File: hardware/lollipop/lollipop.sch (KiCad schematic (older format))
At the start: 24 parts

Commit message: filter/balun bom info
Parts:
- removed T? (x3): BALUN, symbol BALUN
- removed U?: FIL-DEA, symbol FIL-DEA
- removed U?: FIL-LP0603, symbol FIL-LP0603
- added T? (x3): BALUN, symbol BALUN
- added U?: FIL-DEA, symbol FIL-DEA
- added U?: FIL-LP0603, symbol FIL-LP0603
- T?: Description (none) -> BALUN CERAMIC CHIP WIMAX 2.5GHZ; Manufacturer (none) -> Johanson Technology; Part Number (none) -> 2500BL14M100T
- T?: Description (none) -> TRANSFORMR BALUN 2.3-2700MHZ SMD; Manufacturer (none) -> Pulse Electronics; Part Number (none) -> CX2156NL
- T?: Description (none) -> XFMR BALUN RF 3.0-8.0GHZ UWB SMD; Manufacturer (none) -> TDK; Part Number (none) -> HHM1595A1
- U?: Description (none) -> FILTER HIGHPASS WLAN&BLUETOOTH; Manufacturer (none) -> TDK; Part Number (none) -> DEA162400HT-8004B1
- U?: Description (none) -> FILTER LOW PASS 1880MHZ 0603 SMD; Manufacturer (none) -> AVX; Part Number (none) -> LP0603A1880ANTR
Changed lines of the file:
@@
-EESchema Schematic File Version 2  date Sun Apr 22 21:56:01 2012
+EESchema Schematic File Version 2  date Sun Apr 22 22:13:19 2012
 LIBS:power
 LIBS:device
@@
 Comment4 ""
 $EndDescr
+$Comp
+L BALUN T?
+U 1 1 4F94D6C4
+P 7600 6300
+F 0 "T?" H 7600 6550 70  0000 C CNN
+F 1 "BALUN" H 7600 6000 70  0000 C CNN
+F 4 "Pulse Electronics" H 7600 6300 60  0001 C CNN "Manufacturer"
+F 5 "CX2156NL" H 7600 6300 60  0001 C CNN "Part Number"
+F 6 "TRANSFORMR BALUN 2.3-2700MHZ SMD" H 7600 6300 60  0001 C CNN "Description"
+	1    7600 6300
+	-1   0    0    1
+$EndComp
+$Comp
+L BALUN T?
+U 1 1 4F94D601
+P 7600 5500
+F 0 "T?" H 7600 5750 70  0000 C CNN
+F 1 "BALUN" H 7600 5200 70  0000 C CNN
+F 4 "TDK" H 7600 5500 60  0001 C CNN "Manufacturer"
+F 5 "HHM1595A1" H 7600 5500 60  0001 C CNN "Part Number"
+F 6 "XFMR BALUN RF 3.0-8.0GHZ UWB SMD" H 7600 5500 60  0001 C CNN "Description"
+	1    7600 5500
+	-1   0    0    1
+$EndComp
+$Comp
+L BALUN T?
+U 1 1 4F94D59C
+P 7600 7100
+F 0 "T?" H 7600 7350 70  0000 C CNN
+F 1 "BALUN" H 7600 6800 70  0000 C CNN
+F 4 "Johanson Technology" H 7600 7100 60  0001 C CNN "Manufacturer"
+F 5 "2500BL14M100T" H 7600 7100 60  0001 C CNN "Part Number"
+F 6 "BALUN CERAMIC CHIP WIMAX 2.5GHZ" H 7600 7100 60  0001 C CNN "Description"
+	1    7600 7100
+	-1   0    0    1
+$EndComp
+$Comp
+L FIL-LP0603 U?
+U 1 1 4F94D561
+P 6300 6250
+F 0 "U?" H 6300 6300 60  0000 C CNN
+F 1 "FIL-LP0603" H 6300 6200 60  0000 C CNN
+F 4 "AVX" H 6300 6250 60  0001 C CNN "Manufacturer"
+F 5 "LP0603A1880ANTR" H 6300 6250 60  0001 C CNN "Part Number"
+F 6 "FILTER LOW PASS 1880MHZ 0603 SMD" H 6300 6250 60  0001 C CNN "Description"
+	1    6300 6250
+	1    0    0    -1
+$EndComp
+$Comp
+L FIL-DEA U?
+U 1 1 4F94D4F4
+P 6300 5450
+F 0 "U?" H 6300 5500 60  0000 C CNN
+F 1 "FIL-DEA" H 6300 5400 60  0000 C CNN
+F 4 "TDK" H 6300 5450 60  0001 C CNN "Manufacturer"
+F 5 "DEA162400HT-8004B1" H 6300 5450 60  0001 C CNN "Part Number"
+F 6 "FILTER HIGHPASS WLAN&BLUETOOTH" H 6300 5450 60  0001 C CNN "Description"
+	1    6300 5450
+	1    0    0    -1
+$EndComp
 Text Notes 10200 5950 1    400  ~ 0
 mixer
@@
 $Comp
 L FIL-LP0603 U?
-U 1 1 4F94CF87
-P 6300 6250
-F 0 "U?" H 6300 6300 60  0000 C CNN
-F 1 "FIL-LP0603" H 6300 6200 60  0000 C CNN
-	1    6300 6250
-	1    0    0    -1
-$EndComp
-$Comp
-L FIL-DEA U?
-U 1 1 4F94CF80
-P 6300 5450
-F 0 "U?" H 6300 5500 60  0000 C CNN
-F 1 "FIL-DEA" H 6300 5400 60  0000 C CNN
-	1    6300 5450
-	1    0    0    -1
-$EndComp
-$Comp
-L FIL-LP0603 U?
 U 1 1 4F94CF46
 P 6300 3850
 F 0 "U?" H 6300 3900 60  0000 C CNN
 F 1 "FIL-LP0603" H 6300 3800 60  0000 C CNN
+F 4 "AVX" H 6300 3850 60  0001 C CNN "Manufacturer"
+F 5 "LP0603A1880ANTR" H 6300 3850 60  0001 C CNN "Part Number"
+F 6 "FILTER LOW PASS 1880MHZ 0603 SMD" H 6300 3850 60  0001 C CNN "Description"
 	1    6300 3850
 	1    0    0    -1
@@
 F 0 "U?" H 6300 4700 60  0000 C CNN
 F 1 "FIL-DEA" H 6300 4600 60  0000 C CNN
+F 4 "TDK" H 6300 4650 60  0001 C CNN "Manufacturer"
+F 5 "DEA162400HT-8004B1" H 6300 4650 60  0001 C CNN "Part Number"
+F 6 "FILTER HIGHPASS WLAN&BLUETOOTH" H 6300 4650 60  0001 C CNN "Description"
 	1    6300 4650
 	1    0    0    -1
@@
 $Comp
 L BALUN T?
-U 1 1 4F94CC80
-P 7600 7100
-F 0 "T?" H 7600 7350 70  0000 C CNN
-F 1 "BALUN" H 7600 6800 70  0000 C CNN
-	1    7600 7100
-	-1   0    0    1
-$EndComp
-$Comp
-L BALUN T?
-U 1 1 4F94CC7C
-P 7600 6300
-F 0 "T?" H 7600 6550 70  0000 C CNN
-F 1 "BALUN" H 7600 6000 70  0000 C CNN
-	1    7600 6300
-	-1   0    0    1
-$EndComp
-$Comp
-L BALUN T?
-U 1 1 4F94CC75
-P 7600 5500
-F 0 "T?" H 7600 5750 70  0000 C CNN
-F 1 "BALUN" H 7600 5200 70  0000 C CNN
-	1    7600 5500
-	-1   0    0    1
-$EndComp
-$Comp
-L BALUN T?
 U 1 1 4F94CC6F
 P 7600 4700
 F 0 "T?" H 7600 4950 70  0000 C CNN
 F 1 "BALUN" H 7600 4400 70  0000 C CNN
+F 4 "TDK" H 7600 4700 60  0001 C CNN "Manufacturer"
+F 5 "HHM1595A1" H 7600 4700 60  0001 C CNN "Part Number"
+F 6 "XFMR BALUN RF 3.0-8.0GHZ UWB SMD" H 7600 4700 60  0001 C CNN "Description"
 	1    7600 4700
 	-1   0    0    1
@@
 F 0 "T?" H 7600 4150 70  0000 C CNN
 F 1 "BALUN" H 7600 3600 70  0000 C CNN
+F 4 "Pulse Electronics" H 7600 3900 60  0001 C CNN "Manufacturer"
+F 5 "CX2156NL" H 7600 3900 60  0001 C CNN "Part Number"
+F 6 "TRANSFORMR BALUN 2.3-2700MHZ SMD" H 7600 3900 60  0001 C CNN "Description"
 	1    7600 3900
 	-1   0    0    1
@@
 F 0 "T?" H 7600 3350 70  0000 C CNN
 F 1 "BALUN" H 7600 2800 70  0000 C CNN
+F 4 "Johanson Technology" H 7600 3100 60  0001 C CNN "Manufacturer"
+F 5 "2500BL14M100T" H 7600 3100 60  0001 C CNN "Part Number"
+F 6 "BALUN CERAMIC CHIP WIMAX 2.5GHZ" H 7600 3100 60  0001 C CNN "Description"
 	1    7600 3100
 	-1   0    0    1

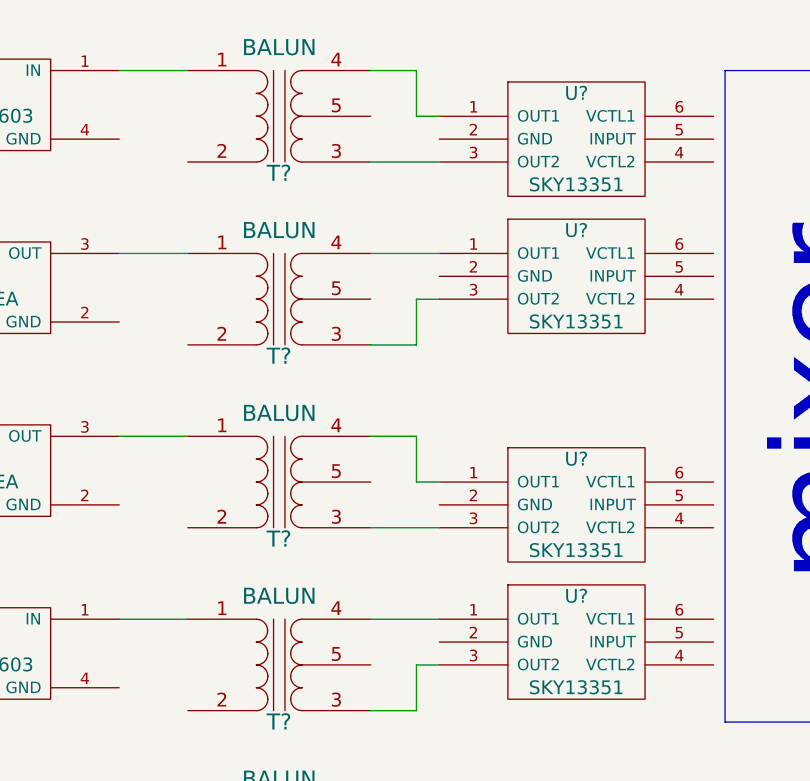
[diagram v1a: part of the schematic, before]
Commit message: fixed balun wiring
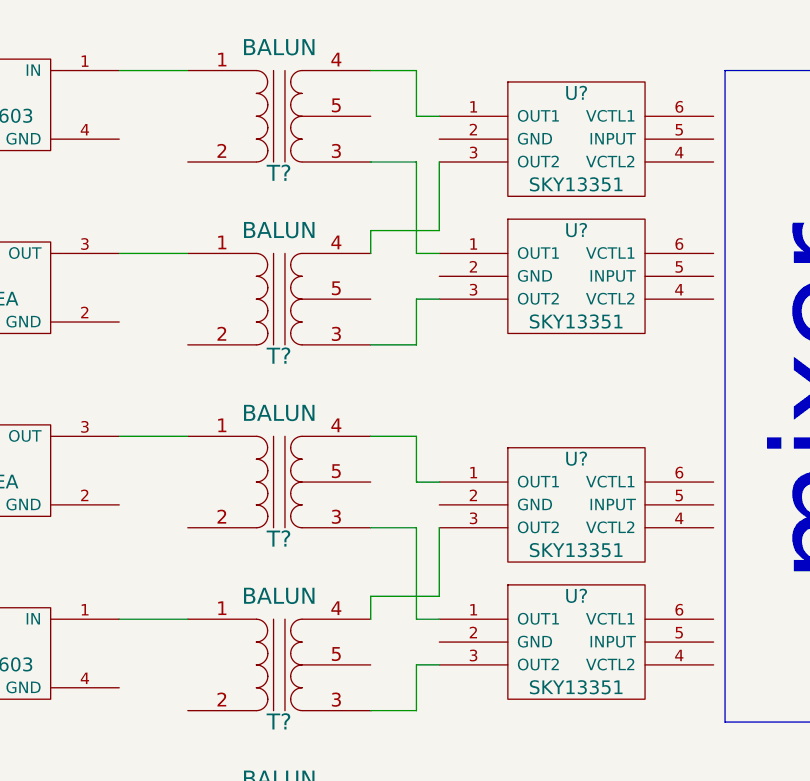
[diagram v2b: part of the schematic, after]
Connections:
- wire segments 69 -> 77
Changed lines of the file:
@@
-EESchema Schematic File Version 2  date Sun Apr 22 22:13:19 2012
+EESchema Schematic File Version 2  date Sun Apr 22 22:20:53 2012
 LIBS:power
 LIBS:device
@@
 Comment4 ""
 $EndDescr
+Wire Wire Line
+	8000 6100 8000 6000
+Wire Wire Line
+	8000 6000 8300 6000
+Wire Wire Line
+	8300 6000 8300 5700
+Wire Wire Line
+	8000 4500 8000 4400
+Wire Wire Line
+	8000 4400 8300 4400
+Wire Wire Line
+	8300 4400 8300 4100
+Wire Bus Line
+	10500 3700 9550 3700
+Wire Bus Line
+	10500 3700 10500 6550
+Wire Bus Line
+	10500 6550 9550 6550
+Wire Bus Line
+	9550 6550 9550 3700
+Wire Wire Line
+	2300 3300 2700 3300
+Wire Wire Line
+	4300 5800 4000 5800
+Wire Wire Line
+	4000 5800 4000 5150
+Wire Wire Line
+	4000 5150 3900 5150
+Wire Wire Line
+	4300 6100 4200 6100
+Wire Wire Line
+	4200 6100 4200 6900
+Wire Wire Line
+	4200 6900 7200 6900
+Wire Wire Line
+	5400 5800 5500 5800
+Wire Wire Line
+	5500 5800 5500 5600
+Wire Wire Line
+	5500 5600 5700 5600
+Wire Wire Line
+	5400 3400 5500 3400
+Wire Wire Line
+	5500 3400 5500 2900
+Wire Wire Line
+	5500 2900 7200 2900
+Wire Wire Line
+	6900 6100 7200 6100
+Wire Wire Line
+	6900 4500 7200 4500
+Wire Wire Line
+	8000 3700 8200 3700
+Wire Wire Line
+	8200 3700 8200 3900
+Wire Wire Line
+	8200 3900 8300 3900
+Wire Wire Line
+	8000 5300 8200 5300
+Wire Wire Line
+	8200 5300 8200 5500
+Wire Wire Line
+	8200 5500 8300 5500
+Wire Wire Line
+	8000 6500 8200 6500
+Wire Wire Line
+	8200 6500 8200 6300
+Wire Wire Line
+	8200 6300 8300 6300
+Wire Wire Line
+	8000 7300 8100 7300
+Wire Wire Line
+	8100 7300 8100 7000
+Wire Wire Line
+	10550 6300 11800 6300
+Wire Wire Line
+	11800 6300 11800 6800
+Wire Wire Line
+	11800 6800 11900 6800
+Wire Wire Line
+	8000 6900 11700 6900
+Wire Wire Line
+	11700 6900 11700 6400
+Wire Wire Line
+	11700 6400 11900 6400
+Wire Wire Line
+	13300 6900 13100 6900
+Wire Wire Line
+	13100 6300 13300 6300
+Wire Wire Line
+	11900 6200 10550 6200
+Wire Wire Line
+	8100 7000 11900 7000
+Wire Wire Line
+	11900 4000 10550 4000
+Wire Wire Line
+	11900 3200 8100 3200
+Wire Wire Line
+	13100 3300 13300 3300
+Wire Wire Line
+	13300 3900 13100 3900
+Wire Wire Line
+	11900 3400 11700 3400
+Wire Wire Line
+	11700 3400 11700 3900
+Wire Wire Line
+	11700 3900 10550 3900
+Wire Wire Line
+	11900 3800 11800 3800
+Wire Wire Line
+	11800 3800 11800 3300
+Wire Wire Line
+	11800 3300 8000 3300
+Wire Wire Line
+	8100 3200 8100 2900
+Wire Wire Line
+	8100 2900 8000 2900
+Wire Wire Line
+	8300 4700 8200 4700
+Wire Wire Line
+	8200 4700 8200 4900
+Wire Wire Line
+	8200 4900 8000 4900
+Wire Wire Line
+	6900 3700 7200 3700
+Wire Wire Line
+	6900 5300 7200 5300
+Wire Wire Line
+	5700 3700 5400 3700
+Wire Wire Line
+	5700 4800 4200 4800
+Wire Wire Line
+	4200 4800 4200 3700
+Wire Wire Line
+	4200 3700 4300 3700
+Wire Wire Line
+	5700 6100 5400 6100
+Wire Wire Line
+	4300 3400 3900 3400
+Wire Wire Line
+	2700 3500 2600 3500
+Wire Wire Line
+	2600 3500 2600 4250
+Wire Wire Line
+	2600 4250 4000 4250
+Wire Wire Line
+	4000 4250 4000 4950
+Wire Wire Line
+	4000 4950 3900 4950
+Wire Wire Line
+	2300 5050 2700 5050
+Wire Wire Line
+	8300 4500 8200 4500
+Wire Wire Line
+	8200 4500 8200 4100
+Wire Wire Line
+	8200 4100 8000 4100
+Wire Wire Line
+	8300 6100 8200 6100
+Wire Wire Line
+	8200 6100 8200 5700
+Wire Wire Line
+	8200 5700 8000 5700
 $Comp
 L BALUN T?
@@
 Text Notes 10200 5950 1    400  ~ 0
 mixer
-Wire Bus Line
-	10500 3700 9550 3700
-Wire Bus Line
-	10500 3700 10500 6550
-Wire Bus Line
-	10500 6550 9550 6550
-Wire Bus Line
-	9550 6550 9550 3700
-Wire Wire Line
-	2300 3300 2700 3300
-Wire Wire Line
-	4300 5800 4000 5800
-Wire Wire Line
-	4000 5800 4000 5150
-Wire Wire Line
-	4000 5150 3900 5150
-Wire Wire Line
-	4300 6100 4200 6100
-Wire Wire Line
-	4200 6100 4200 6900
-Wire Wire Line
-	4200 6900 7200 6900
-Wire Wire Line
-	5400 5800 5500 5800
-Wire Wire Line
-	5500 5800 5500 5600
-Wire Wire Line
-	5500 5600 5700 5600
-Wire Wire Line
-	5400 3400 5500 3400
-Wire Wire Line
-	5500 3400 5500 2900
-Wire Wire Line
-	5500 2900 7200 2900
-Wire Wire Line
-	6900 6100 7200 6100
-Wire Wire Line
-	6900 4500 7200 4500
-Wire Wire Line
-	8000 3700 8200 3700
-Wire Wire Line
-	8200 3700 8200 3900
-Wire Wire Line
-	8200 3900 8300 3900
-Wire Wire Line
-	8300 4500 8000 4500
-Wire Wire Line
-	8000 5300 8200 5300
-Wire Wire Line
-	8200 5300 8200 5500
-Wire Wire Line
-	8200 5500 8300 5500
-Wire Wire Line
-	8000 6500 8200 6500
-Wire Wire Line
-	8200 6500 8200 6300
-Wire Wire Line
-	8200 6300 8300 6300
-Wire Wire Line
-	8000 7300 8100 7300
-Wire Wire Line
-	8100 7300 8100 7000
-Wire Wire Line
-	10550 6300 11800 6300
-Wire Wire Line
-	11800 6300 11800 6800
-Wire Wire Line
-	11800 6800 11900 6800
-Wire Wire Line
-	8000 6900 11700 6900
-Wire Wire Line
-	11700 6900 11700 6400
-Wire Wire Line
-	11700 6400 11900 6400
-Wire Wire Line
-	13300 6900 13100 6900
-Wire Wire Line
-	13100 6300 13300 6300
-Wire Wire Line
-	11900 6200 10550 6200
-Wire Wire Line
-	8100 7000 11900 7000
-Wire Wire Line
-	11900 4000 10550 4000
-Wire Wire Line
-	11900 3200 8100 3200
-Wire Wire Line
-	13100 3300 13300 3300
-Wire Wire Line
-	13300 3900 13100 3900
-Wire Wire Line
-	11900 3400 11700 3400
-Wire Wire Line
-	11700 3400 11700 3900
-Wire Wire Line
-	11700 3900 10550 3900
-Wire Wire Line
-	11900 3800 11800 3800
-Wire Wire Line
-	11800 3800 11800 3300
-Wire Wire Line
-	11800 3300 8000 3300
-Wire Wire Line
-	8100 3200 8100 2900
-Wire Wire Line
-	8100 2900 8000 2900
-Wire Wire Line
-	8300 6100 8000 6100
-Wire Wire Line
-	8300 5700 8000 5700
-Wire Wire Line
-	8300 4700 8200 4700
-Wire Wire Line
-	8200 4700 8200 4900
-Wire Wire Line
-	8200 4900 8000 4900
-Wire Wire Line
-	8300 4100 8000 4100
-Wire Wire Line
-	6900 3700 7200 3700
-Wire Wire Line
-	6900 5300 7200 5300
-Wire Wire Line
-	5700 3700 5400 3700
-Wire Wire Line
-	5700 4800 4200 4800
-Wire Wire Line
-	4200 4800 4200 3700
-Wire Wire Line
-	4200 3700 4300 3700
-Wire Wire Line
-	5700 6100 5400 6100
-Wire Wire Line
-	4300 3400 3900 3400
-Wire Wire Line
-	2700 3500 2600 3500
-Wire Wire Line
-	2600 3500 2600 4250
-Wire Wire Line
-	2600 4250 4000 4250
-Wire Wire Line
-	4000 4250 4000 4950
-Wire Wire Line
-	4000 4950 3900 4950
-Wire Wire Line
-	2300 5050 2700 5050
 $Comp
 L GSG-SMA-CONN P?

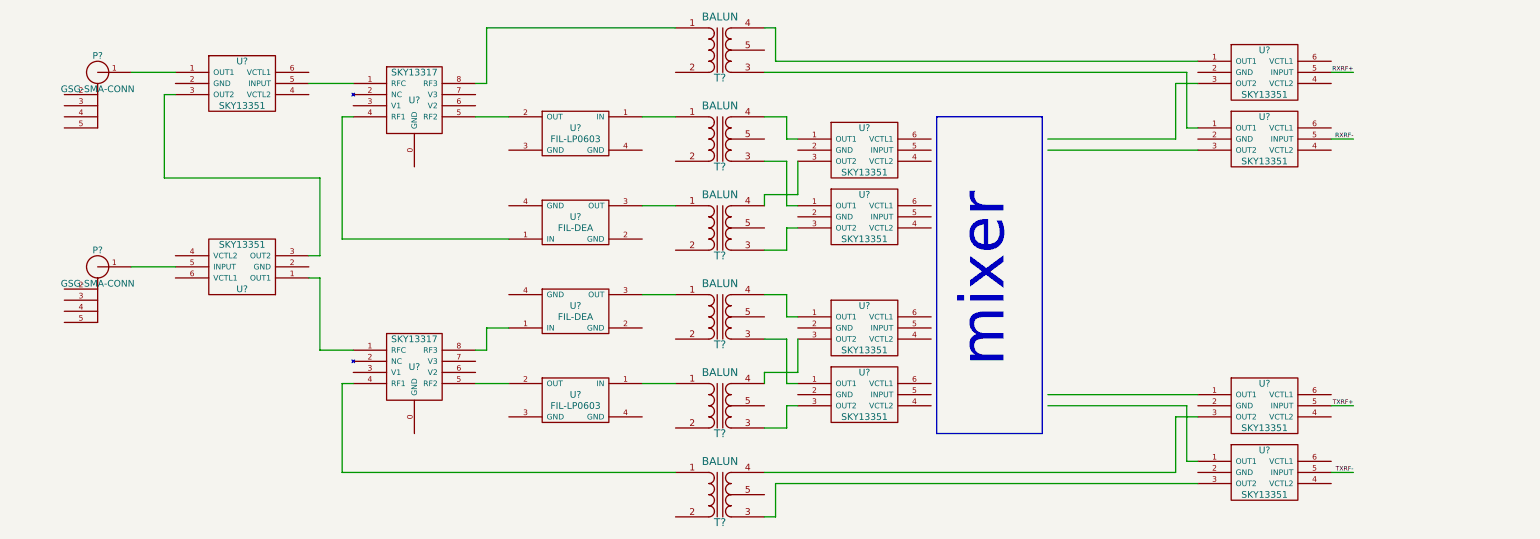
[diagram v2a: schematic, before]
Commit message: added RFFC5071
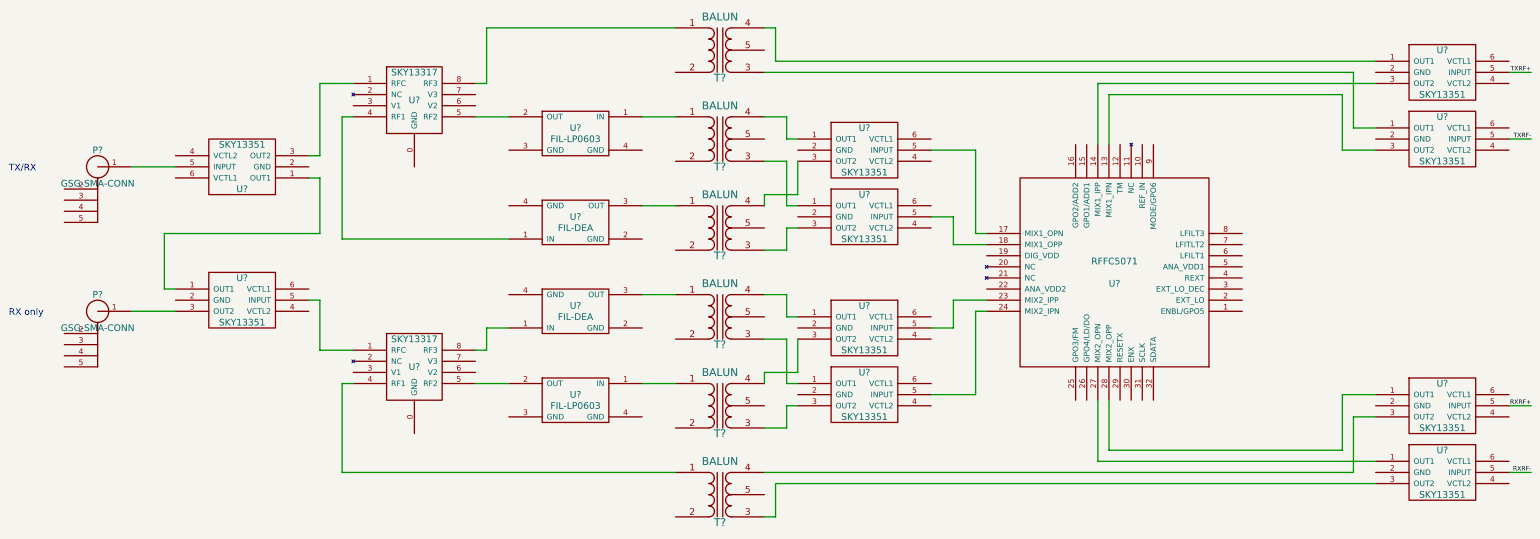
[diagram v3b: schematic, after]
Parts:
- added U?: RFFC5071, symbol RFFC5071
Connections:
- wire segments 77 -> 95
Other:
- note added: "RX only"
- note added: "TX/RX"
- note removed: "mixer"
- moved on the sheet: P?, U?

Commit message: started adding switch blocking and bypass caps
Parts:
- added C? (x2): 33pF, symbol C
- added C? (x3): 100pF, symbol C
- added P?: TX-IN, symbol GSG-SMA-CONN
- added P?: RX-OUT, symbol GSG-SMA-CONN
- added T? (x2): BALUN, symbol BALUN
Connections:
- net RXRF+: now also T?.3 (PR1)
- net RXRF-: now also T?.4 (PR2)
- net TXRF-: now also T?.4 (PR2)
- net at U?.1 (OUT1): now also C?.2; no longer T?.4 (PR2)
- net GND: now reaches U?.2 (GND)
- net GND: now also C?.1, C?.2, T?.1 (S1)
- net at U?.3 (OUT2): now also C?.1; no longer U?.14 (MIX1_IPP)
- net SWTXB2: now reaches U?.4 (VCTL2)
- net SWTXB2: now also C?.2
- net SWTXB1: now reaches U?.6 (VCTL1)
- net SWTXB1: now also C?.1
- net TXRF+: no longer names the net of U?.5 (INPUT)
- net TXRF+: now also C?.1
- new net: C?.1, T?.4 (PR2)
- new net: C?.2, U?.14 (MIX1_IPP)
- new net: P?.1 (RF), T?.2 (S2) (x2)
- new net: C?.2, T?.3 (PR1)
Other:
- moved on the sheet: P?, T?, U?

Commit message: finished switch blocking and bypass caps
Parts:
- removed T?: BALUN, symbol BALUN
- removed U? (x8): SKY13351, symbol SKY13351
- added C? (x18): 33pF, symbol C
- added C? (x27): 100pF, symbol C
- added C? (x6): 47pF, symbol C
- added T?: BALUN, symbol BALUN
- added U? (x8): SKY13351, symbol SKY13351
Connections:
- net GND: now also C?.2, P?.2 (GND), P?.2 (GND), P?.2 (GND), P?.2 (GND), P?.3 (GND), P?.3 (GND), P?.3 (GND), P?.3 (GND), P?.4 (GND), P?.4 (GND), P?.4 (GND), P?.4 (GND), P?.5 (GND), P?.5 (GND), P?.5 (GND), P?.5 (GND), T?.2 (S2), T?.2 (S2), T?.2 (S2), T?.2 (S2), T?.2 (S2), T?.2 (S2), T?.5 (PM), T?.5 (PM), T?.5 (PM), T?.5 (PM), T?.5 (PM), T?.5 (PM), T?.5 (PM), U?.0 (GND), U?.0 (GND), U?.2 (GND), U?.2 (GND), U?.2 (GND), U?.3 (GND), U?.3 (GND), U?.4 (GND), U?.4 (GND), U?.4 (GND), U?.4 (GND), C?.2, C?.2, C?.2, C?.2, C?.2, C?.2, C?.2, C?.2, C?.2, C?.2, C?.2, C?.2, C?.2, C?.2, C?.2, C?.2, C?.2, C?.2, T?.1 (S1), T?.5 (PM), U?.2 (GND), U?.2 (GND), U?.2 (GND), U?.2 (GND), U?.2 (GND), U?.2 (GND), U?.2 (GND), U?.2 (GND); no longer C?.1
- net SWTXB1: now also U?.6 (VCTL1), C?.1
- net SWTXB2: now also C?.1, U?.4 (VCTL2), C?.1; no longer C?.2
- net at U?.1 (RFC): now also C?.2
- net SWRXV1: now reaches U?.3 (V1)
- net at U?.4 (RF1): now also C?.1; no longer T?.1 (S1)
- net at U?.5 (RF2): now also C?.2; no longer U?.2 (OUT)
- net SWRXV2: now reaches U?.6 (V2)
- net SWRXV3: now reaches U?.7 (V3)
- net at U?.8 (RF3): now also C?.2; no longer U?.1 (IN)
- net at U?.1 (OUT1): now also C?.2; no longer T?.3 (PR1)
- net at U?.3 (OUT2): now also C?.1; no longer U?.13 (MIX1_IPN)
- net at U?.27 (MIX2_OPN): now also C?.1
- net at T?.3 (PR1): now also C?.2 (x3)
- net at U?.28 (MIX2_OPP): now also C?.1
- net at T?.4 (PR2): now also C?.2 (x3)
- net at T?.1 (S1): now also C?.2; no longer U?.8 (RF3)
- net at T?.3 (PR1): now also C?.1 (x2)
- net at T?.4 (PR2): now also C?.1 (x2)
- net at U?.18 (MIX1_OPP): now also C?.2
- net at U?.17 (MIX1_OPN): now also C?.2
- net at U?.23 (MIX2_IPP): now also C?.2
- net at U?.24 (MIX2_IPN): now also C?.2
- net at U?.1 (IN): now also C?.2; no longer U?.4 (RF1)
- net at U?.2 (OUT): now also C?.2; no longer U?.5 (RF2)
- net at U?.1 (RFC): now also C?.1
- net SWTXV1: now reaches U?.3 (V1)
- net SWTXV2: now reaches U?.6 (V2)
- net SWTXV3: now reaches U?.7 (V3)
- net at P?.1 (RF): now also C?.2 (x2)
- net VCC: now reaches U?.19 (DIG_VDD)
- net VCC: now also U?.22 (ANA_VDD2)
- net at P?.1 (RF): now also T?.2 (S2)
- net TXRF-: no longer names the net of U?.5 (INPUT)
- net TXRF-: now also C?.1; no longer T?.4 (PR2)
- new net: C?.1, T?.3 (PR1)
- new net: C?.1, U?.4 (RF1)
- new net: C?.1, U?.5 (RF2)
- new net: C?.1, U?.8 (RF3)
- new net: C?.1, U?.1 (IN)
- new net: C?.1, U?.2 (OUT)
- new net: C?.2, T?.1 (S1)
- new net: C?.2, U?.13 (MIX1_IPN)
- new net: C?.2, T?.4 (PR2) (x2)
- new net: C?.1, U?.3 (OUT2) (x8)
- new net: C?.2, U?.1 (OUT1) (x8)
- new net: C?.1, U?.5 (INPUT) (x8)
- new net: C?.2, T?.3 (PR1)
- new net: C?.1, C?.2
- new net SWD1: C?.1, C?.1, U?.4 (VCTL2), U?.6 (VCTL1)
- new net SWD2: C?.1, C?.1, U?.4 (VCTL2), U?.6 (VCTL1)
- new net SWRXA1: C?.1, C?.1, U?.6 (VCTL1), U?.6 (VCTL1)
- new net SWRXA2: C?.1, C?.1, U?.4 (VCTL2), U?.4 (VCTL2)
- new net SWRXB1: C?.1, C?.1, U?.6 (VCTL1), U?.6 (VCTL1)
- new net SWRXB2: C?.1, C?.1, U?.4 (VCTL2), U?.4 (VCTL2)
- new net SWTXA1: C?.1, C?.1, U?.6 (VCTL1), U?.6 (VCTL1)
- new net SWTXA2: C?.1, C?.1, U?.4 (VCTL2), U?.4 (VCTL2)
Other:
- moved on the sheet: C?, P?, T?, U?
